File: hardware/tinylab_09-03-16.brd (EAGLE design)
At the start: 201.3 x 116.2 mm, 151 parts, among them IC1 LM2575S, IC2 LM35CZ, IC3 LM358MX, IC4 MCP2300X/SO, IC5 LD117AS33TR, IC6 MAX7219CWG, J1 AVR_SPI_PRG_6NS, J2 POWER_JACKPTH_LOCK, K4 ZF112, M1 WIRELESS-NRF24L01, P1 P120PK, Q1 FDD4141 or FDD6637, Q3 BSS138, Q4 BSS138, SW1 ENCODER_SW1-PEC12, U1 LCD-16X2SILK, U2 24LC256, U5 USD-SOCKETNEW, Y1 16Mhz

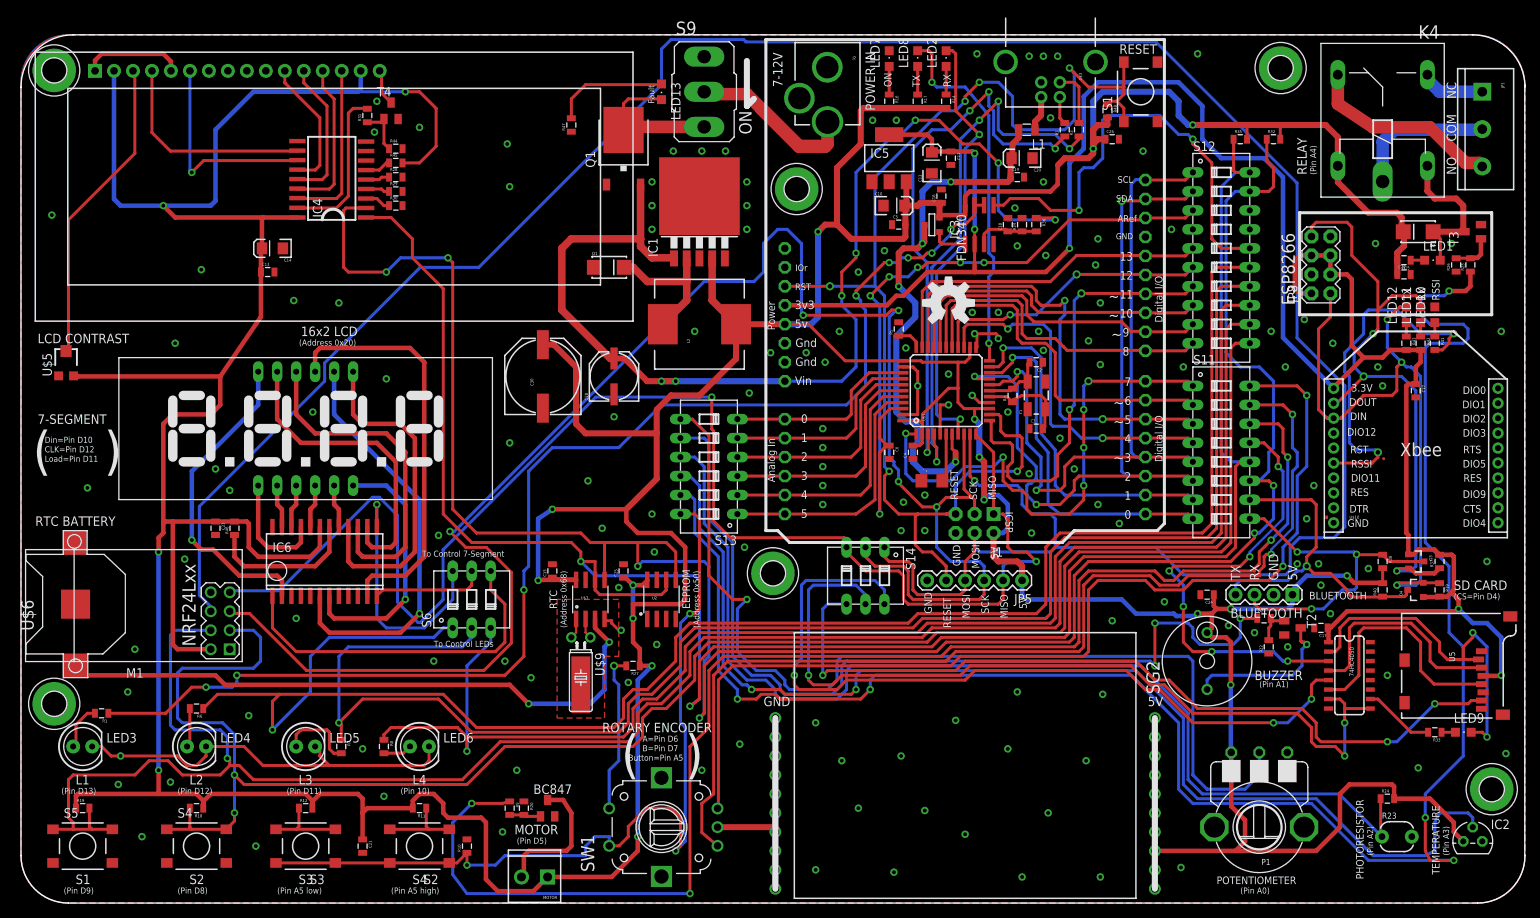
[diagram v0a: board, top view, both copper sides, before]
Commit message: added resistor on lcd backlight led and done some  little changes.
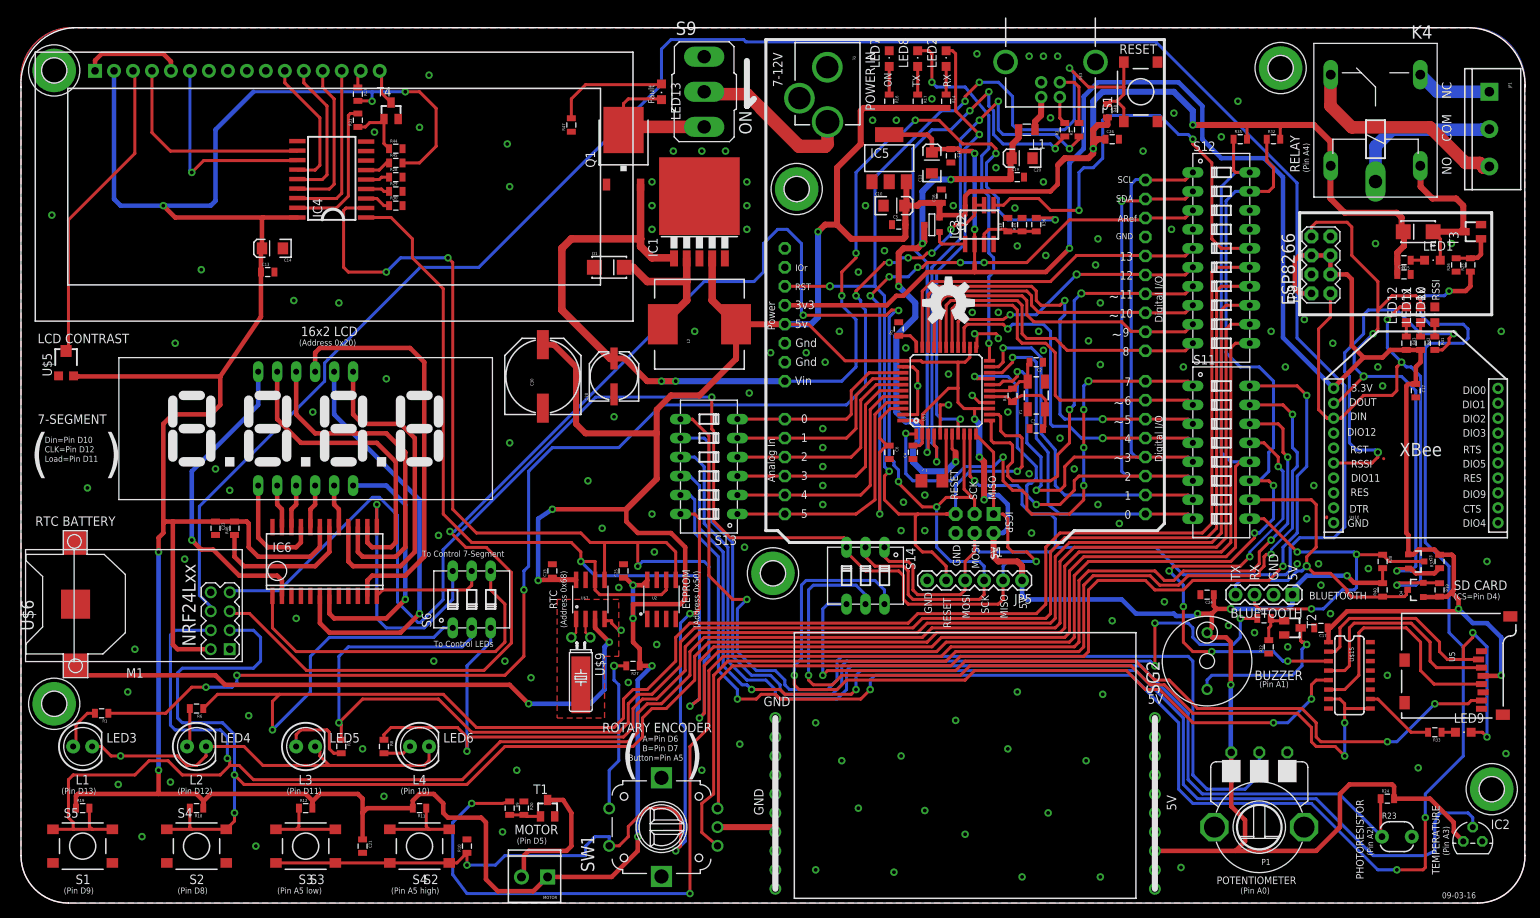
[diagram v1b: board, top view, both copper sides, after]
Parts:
- removed U$8: (no value), tinylab_logo:INDIEGOGO_FONT_LOGO
- added R13: 100R, SparkFun:0805
- C21, C25: value 100n -> 100nF
- LED3, LED4, LED5, LED6: value (none) -> RED
- Q2: value (none) -> FDN340
- R46: value 30k civari -> 30k
- T1, T2, T3, T4: value (none) -> BC847
- U$15: value HEX_CONVERTER -> 74HC4050
- moved R31 1.42 mm to (42.5, 103.5)
- moved JP1 0.95 mm to (194.0, 107.3)
- moved K4 0.95 mm to (178.8, 103.5)
- moved C11 0.32 mm to (121.9, 98.7)
- renumbered 74HC4050 to U$15, BC847 to T1, FDN340 to Q2
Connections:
- new net N$65: R13.1, U1.15
- net +5V: now also R13.2; no longer U1.15
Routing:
- net A4: track 247.2 -> 241.7 mm
- net N$65: track 0.00 -> 2.38 mm
- net N$14: track 27.1 -> 29.2 mm
- net VCC: track 147.8 -> 149.8 mm
- net LIGHT: track 21.4 -> 19.7 mm
- net N$33: track 6.67 -> 8.20 mm
- net N$25: track 8.67 -> 10.2 mm
- net N$24: track 19.4 -> 20.9 mm
- net +5V: track 975.9 -> 977.1 mm, vias 30 -> 31
- net TXLED: track 48.9 -> 49.7 mm
- net N$21: track 21.2 -> 21.8 mm
- net GND: vias 162 -> 168
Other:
- board size 201.3 x 116.2 mm -> 201.3 x 117.2 mm
- board text added: "09-03-16"
- board text added: "Designed by: Yusuf Gundogdu"
- board text added: "Released under the GNU-GPL v2"
- board text added: "Revised by: Okan Saracoglu"
- board text added: "XBee"
- board text added: "https://www.tinylab.cc"
- board text removed: "Xbee"
